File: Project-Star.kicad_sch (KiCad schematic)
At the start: 0 parts

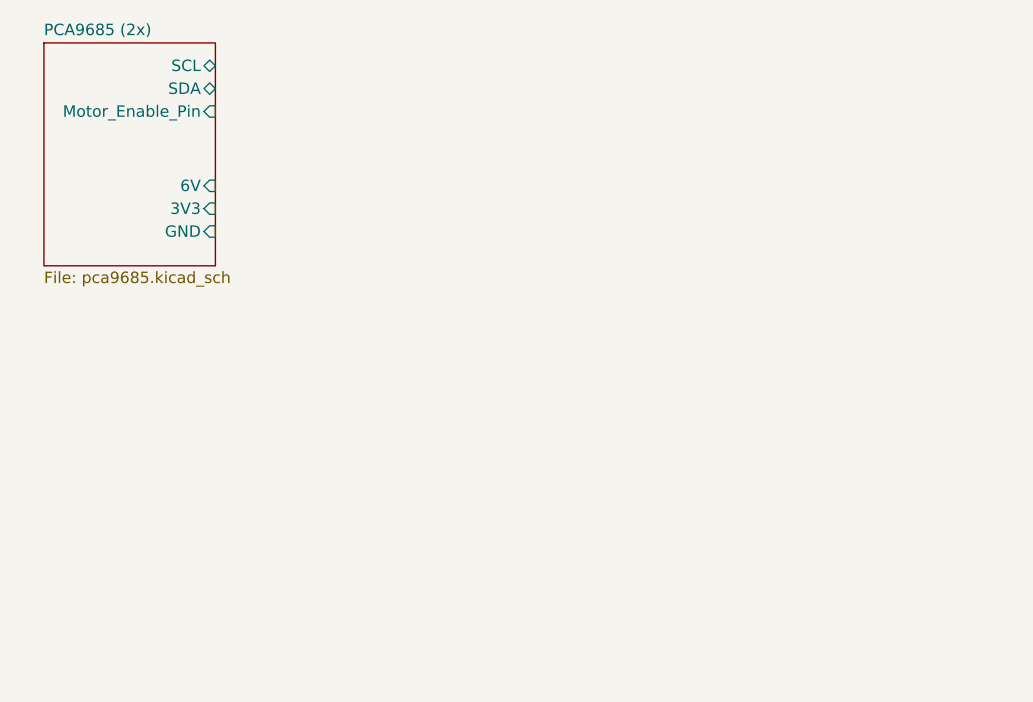
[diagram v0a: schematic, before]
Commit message: added 3v3 line
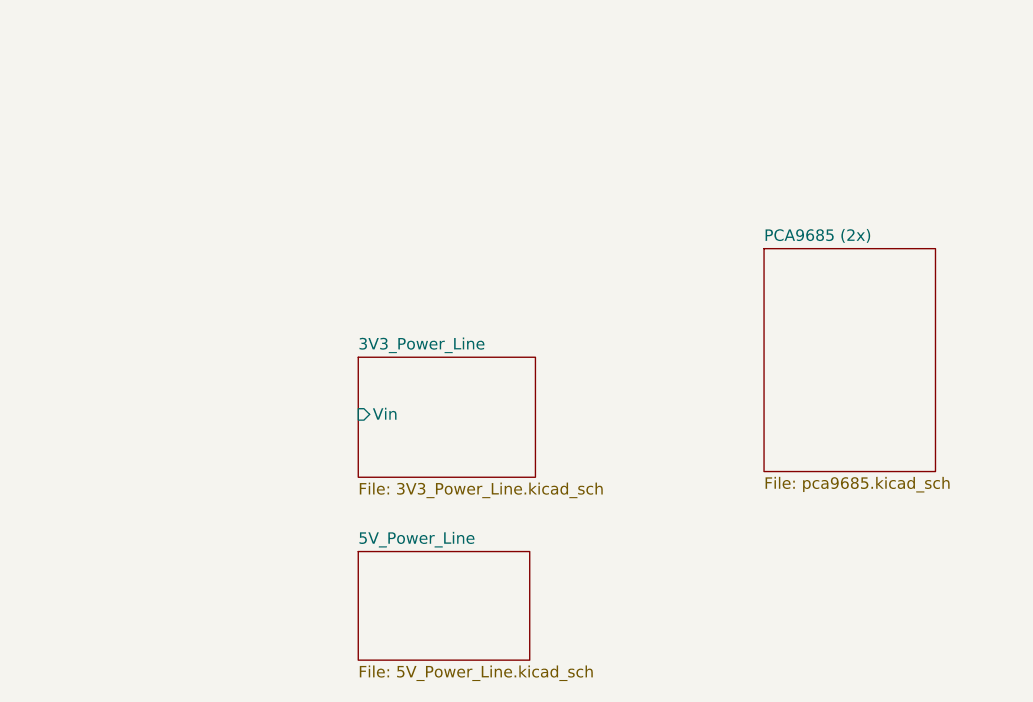
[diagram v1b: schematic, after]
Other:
- added sheet 3V3_Power_Line (3V3_Power_Line.kicad_sch)
- added sheet 5V_Power_Line (5V_Power_Line.kicad_sch)
- sheet PCA9685 (2x) ports: added none; removed 3V3, 6V, GND, Motor_Enable_Pin, SCL, SDA
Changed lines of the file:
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@@
 	(paper "A4")
 	(sheet
-		(at 20.32 20.955)
+		(at 55.245 55.88)
+		(size 19.685 13.335)
+		(exclude_from_sim no)
+		(in_bom yes)
+		(on_board yes)
+		(dnp no)
+		(fields_autoplaced yes)
+		(stroke
+			(width 0.1524)
+			(type solid)
+		)
+		(fill
+			(color 0 0 0 0.0000)
+		)
+		(property "Sheetname" "3V3_Power_Line"
+			(at 55.245 55.1684 0)
+			(effects
+				(font
+					(size 1.27 1.27)
+				)
+				(justify left bottom)
+			)
+		)
+		(property "Sheetfile" "3V3_Power_Line.kicad_sch"
+			(at 55.245 69.7996 0)
+			(effects
+				(font
+					(size 1.27 1.27)
+				)
+				(justify left top)
+			)
+		)
+		(pin "Vin" input
+			(at 55.245 62.23 180)
+			(effects
+				(font
+					(size 1.27 1.27)
+				)
+				(justify left)
+			)
+		)
+		(instances
+			(project "Project-Star"
+				(path "/dfa3d008-01ec-4328-886a-a4a57a49a859"
+					(page "4")
+				)
+			)
+		)
+	)
+	(sheet
+		(at 55.245 77.47)
+		(size 19.05 12.065)
+		(exclude_from_sim no)
+		(in_bom yes)
+		(on_board yes)
+		(dnp no)
+		(fields_autoplaced yes)
+		(stroke
+			(width 0.1524)
+			(type solid)
+		)
+		(fill
+			(color 0 0 0 0.0000)
+		)
+		(property "Sheetname" "5V_Power_Line"
+			(at 55.245 76.7584 0)
+			(effects
+				(font
+					(size 1.27 1.27)
+				)
+				(justify left bottom)
+			)
+		)
+		(property "Sheetfile" "5V_Power_Line.kicad_sch"
+			(at 55.245 90.1196 0)
+			(effects
+				(font
+					(size 1.27 1.27)
+				)
+				(justify left top)
+			)
+		)
+		(instances
+			(project "Project-Star"
+				(path "/dfa3d008-01ec-4328-886a-a4a57a49a859"
+					(page "5")
+				)
+			)
+		)
+	)
+	(sheet
+		(at 100.33 43.815)
 		(size 19.05 24.765)
 		(exclude_from_sim no)
@@
 		)
 		(property "Sheetname" "PCA9685 (2x)"
-			(at 20.32 20.2434 0)
+			(at 100.33 43.1034 0)
 			(effects
 				(font
@@
 		)
 		(property "Sheetfile" "pca9685.kicad_sch"
-			(at 20.32 46.3046 0)
+			(at 100.33 69.1646 0)
 			(effects
 				(font
@@
 			)
 		)
-		(pin "SCL" bidirectional
-			(at 39.37 23.495 0)
-			(effects
-				(font
-					(size 1.27 1.27)
-				)
-				(justify right)
-			)
-		)
-		(pin "Motor_Enable_Pin" input
-			(at 39.37 28.575 0)
-			(effects
-				(font
-					(size 1.27 1.27)
-				)
-				(justify right)
-			)
-		)
-		(pin "SDA" bidirectional
-			(at 39.37 26.035 0)
-			(effects
-				(font
-					(size 1.27 1.27)
-				)
-				(justify right)
-			)
-		)
-		(pin "GND" input
-			(at 39.37 41.91 0)
-			(effects
-				(font
-					(size 1.27 1.27)
-				)
-				(justify right)
-			)
-		)
-		(pin "6V" input
-			(at 39.37 36.83 0)
-			(effects
-				(font
-					(size 1.27 1.27)
-				)
-				(justify right)
-			)
-		)
-		(pin "3V3" input
-			(at 39.37 39.37 0)
-			(effects
-				(font
-					(size 1.27 1.27)
-				)
-				(justify right)
-			)
-		)
 		(instances
 			(project "Project-Star"
 				(path "/dfa3d008-01ec-4328-886a-a4a57a49a859"
-					(page "3")
+					(page "2")
 				)
 			)

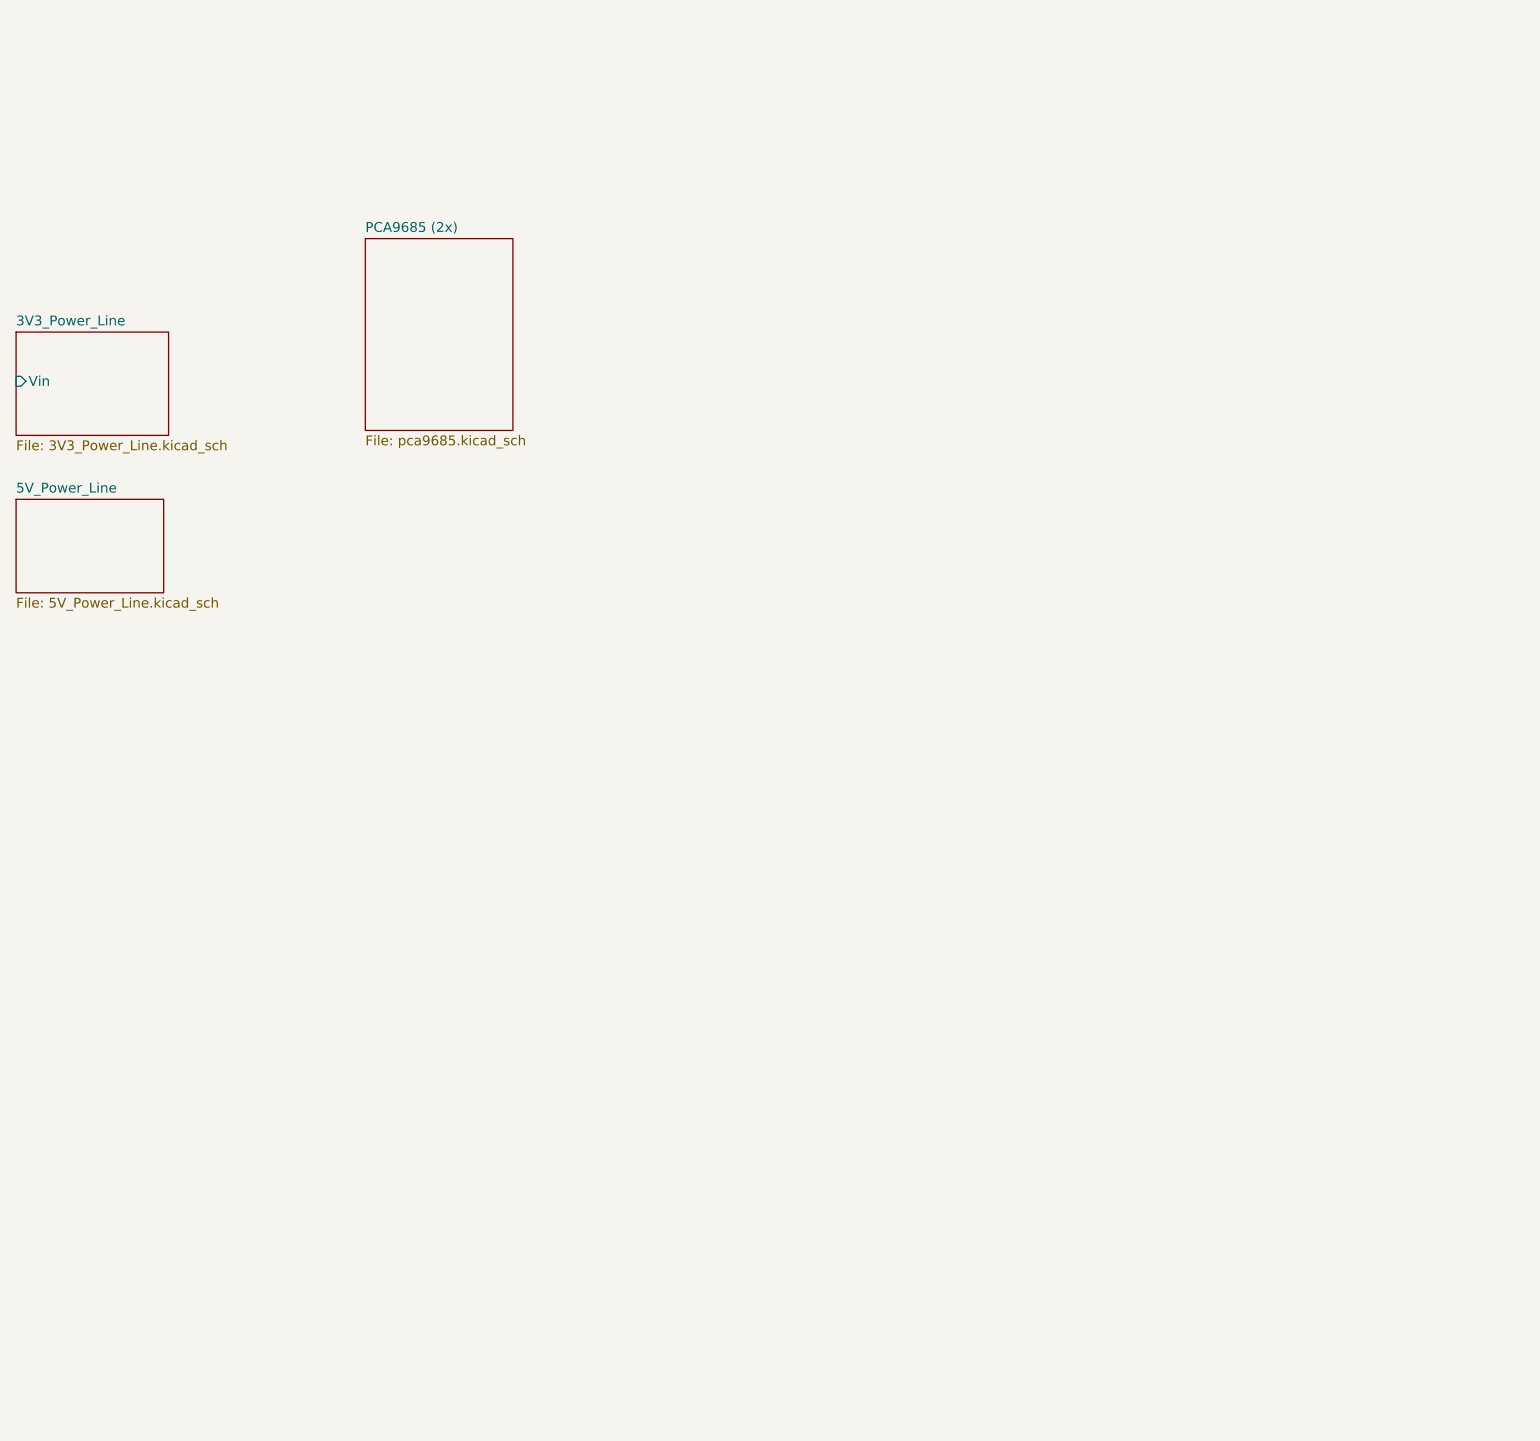
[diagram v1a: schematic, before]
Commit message: added more power lines
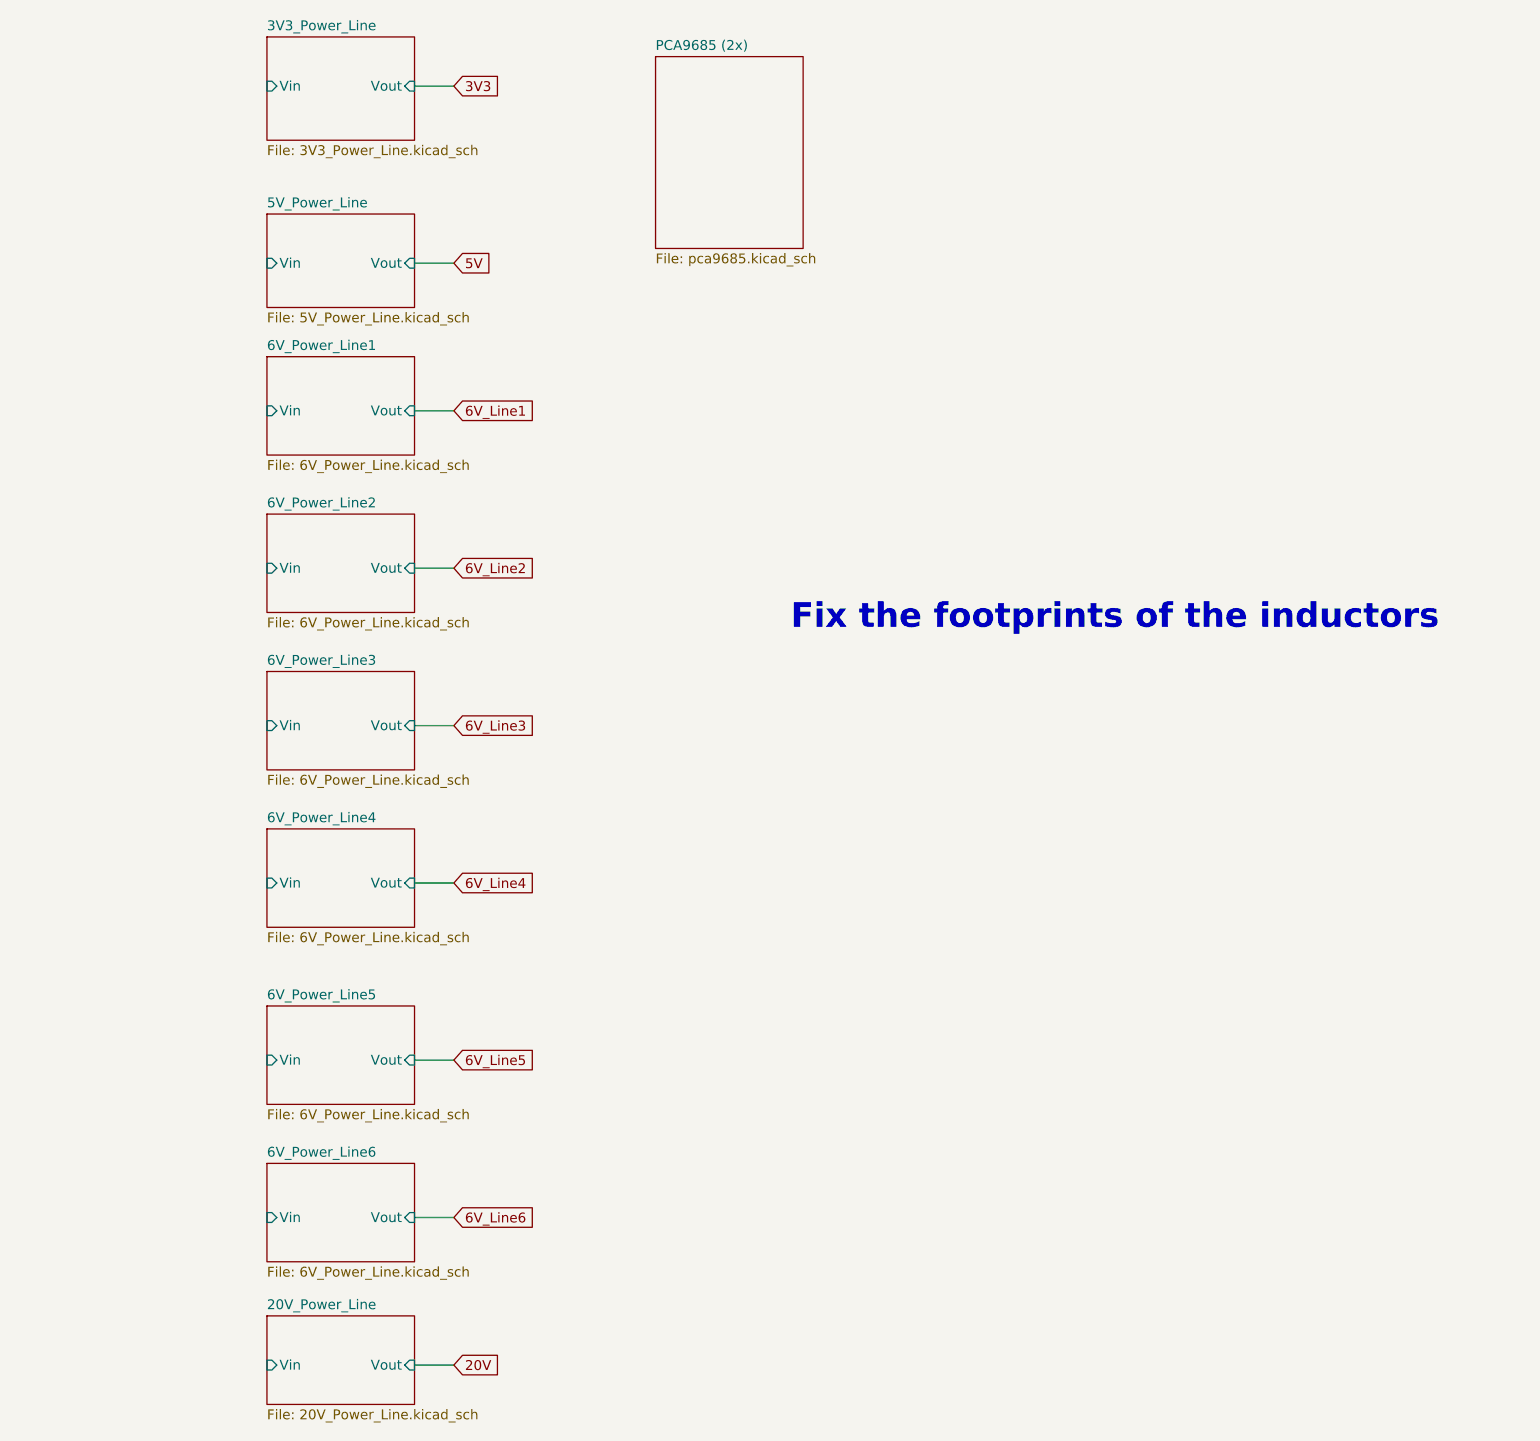
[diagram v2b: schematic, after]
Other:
- added sheet 20V_Power_Line (20V_Power_Line.kicad_sch)
- added sheet 6V_Power_Line1 (6V_Power_Line.kicad_sch)
- added sheet 6V_Power_Line2 (6V_Power_Line.kicad_sch)
- added sheet 6V_Power_Line3 (6V_Power_Line.kicad_sch)
- added sheet 6V_Power_Line4 (6V_Power_Line.kicad_sch)
- added sheet 6V_Power_Line5 (6V_Power_Line.kicad_sch)
- added sheet 6V_Power_Line6 (6V_Power_Line.kicad_sch)
- sheet 3V3_Power_Line ports: added Vout; removed none
- sheet 5V_Power_Line ports: added Vin, Vout; removed none
- note added: "Fix the footprints of the inductors"
